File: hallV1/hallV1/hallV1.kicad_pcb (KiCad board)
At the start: 2 copper layers, 13 x 8 mm, 3 parts, among them J1 Conn_01x03_Female, U1 AH1806-Z

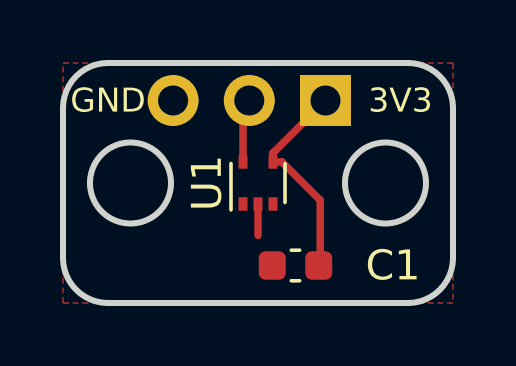
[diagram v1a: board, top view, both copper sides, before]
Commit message: Change decoupling capacitor position
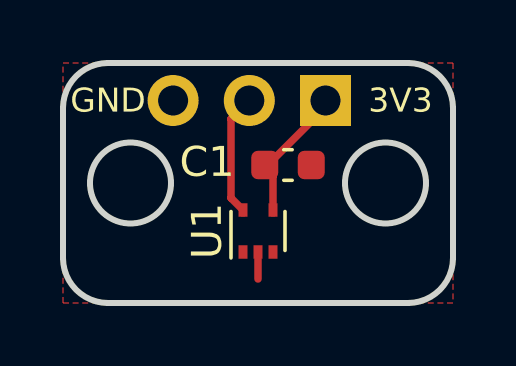
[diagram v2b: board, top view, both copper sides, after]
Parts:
- moved C1 3.36 mm to (105.2, 99.4), turned to 0 degrees
- moved U1 1.60 mm to (104.2, 101.6)
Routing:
- net +3V3: track 7.05 -> 4.70 mm
- net Net-(J1-Pad2): track 2.14 -> 4.47 mm
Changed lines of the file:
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@@
     (thickness 1)
     (drawings 13)
-    (tracks 8)
+    (tracks 10)
     (zones 0)
     (modules 3)
@@
     (aux_axis_origin 0 0)
     (grid_origin 97.75 104)
-    (visible_elements FFFFFF7F)
+    (visible_elements 7FFFFFFF)
     (pcbplotparams
       (layerselection 0x010fc_ffffffff)
@@
   )
   (module Capacitor_SMD:C_0603_1608Metric (layer F.Cu)
-    (at 105.5 102.75 180)
+    (at 105.25 99.4)
     (descr "Capacitor SMD 0603 (1608 Metric), square (rectangular) end terminal, IPC_7351 nominal, (Body size source: IPC-SM-782 page 76, https://www.pcb-3d.com/wordpress/wp-content/uploads/ipc-sm-782a_amendment_1_and_2.pdf), generated with kicad-footprint-generator")
     (tags capacitor)
     (attr smd)
-    (fp_text reference C1 (at -3.25 0) (layer F.SilkS)
+    (fp_text reference C1 (at -2.7 -0.1) (layer F.SilkS)
       (effects (font (size 1 1) (thickness 0.15)))
     )
@@
       (effects (font (size 1 1) (thickness 0.15)))
     )
+    (fp_line (start 1.48 0.73) (end -1.48 0.73) (layer F.CrtYd) (width 0.05))
+    (fp_line (start 1.48 -0.73) (end 1.48 0.73) (layer F.CrtYd) (width 0.05))
+    (fp_line (start -1.48 -0.73) (end 1.48 -0.73) (layer F.CrtYd) (width 0.05))
+    (fp_line (start -1.48 0.73) (end -1.48 -0.73) (layer F.CrtYd) (width 0.05))
+    (fp_line (start -0.14058 0.51) (end 0.14058 0.51) (layer F.SilkS) (width 0.12))
+    (fp_line (start -0.14058 -0.51) (end 0.14058 -0.51) (layer F.SilkS) (width 0.12))
+    (fp_line (start 0.8 0.4) (end -0.8 0.4) (layer F.Fab) (width 0.1))
+    (fp_line (start 0.8 -0.4) (end 0.8 0.4) (layer F.Fab) (width 0.1))
+    (fp_line (start -0.8 -0.4) (end 0.8 -0.4) (layer F.Fab) (width 0.1))
+    (fp_line (start -0.8 0.4) (end -0.8 -0.4) (layer F.Fab) (width 0.1))
     (fp_text user %R (at 0 0) (layer F.Fab)
       (effects (font (size 0.4 0.4) (thickness 0.06)))
     )
-    (fp_line (start -0.8 0.4) (end -0.8 -0.4) (layer F.Fab) (width 0.1))
-    (fp_line (start -0.8 -0.4) (end 0.8 -0.4) (layer F.Fab) (width 0.1))
-    (fp_line (start 0.8 -0.4) (end 0.8 0.4) (layer F.Fab) (width 0.1))
-    (fp_line (start 0.8 0.4) (end -0.8 0.4) (layer F.Fab) (width 0.1))
-    (fp_line (start -0.14058 -0.51) (end 0.14058 -0.51) (layer F.SilkS) (width 0.12))
-    (fp_line (start -0.14058 0.51) (end 0.14058 0.51) (layer F.SilkS) (width 0.12))
-    (fp_line (start -1.48 0.73) (end -1.48 -0.73) (layer F.CrtYd) (width 0.05))
-    (fp_line (start -1.48 -0.73) (end 1.48 -0.73) (layer F.CrtYd) (width 0.05))
-    (fp_line (start 1.48 -0.73) (end 1.48 0.73) (layer F.CrtYd) (width 0.05))
-    (fp_line (start 1.48 0.73) (end -1.48 0.73) (layer F.CrtYd) (width 0.05))
-    (pad 2 smd roundrect (at 0.775 0 180) (size 0.9 0.95) (layers F.Cu F.Paste F.Mask) (roundrect_rratio 0.25)
+    (pad 2 smd roundrect (at 0.775 0) (size 0.9 0.95) (layers F.Cu F.Paste F.Mask) (roundrect_rratio 0.25)
       (net 1 GND))
-    (pad 1 smd roundrect (at -0.775 0 180) (size 0.9 0.95) (layers F.Cu F.Paste F.Mask) (roundrect_rratio 0.25)
+    (pad 1 smd roundrect (at -0.775 0) (size 0.9 0.95) (layers F.Cu F.Paste F.Mask) (roundrect_rratio 0.25)
       (net 2 +3V3))
     (model ${KISYS3DMOD}/Capacitor_SMD.3dshapes/C_0603_1608Metric.wrl
@@
       (effects (font (size 1 1) (thickness 0.15)) (justify mirror))
     )
+    (fp_line (start -1.27 1.27) (end 0 1.27) (layer B.SilkS) (width 0.12))
     (fp_line (start -1.27 0) (end -1.27 1.27) (layer B.SilkS) (width 0.12))
-    (fp_line (start -1.27 1.27) (end 0 1.27) (layer B.SilkS) (width 0.12))
     (pad 3 thru_hole oval (at 0 -5.08 90) (size 1.7 1.7) (drill 1) (layers *.Cu *.Mask)
       (net 1 GND))
@@
   )
   (module Package_TO_SOT_SMD:SOT-553 (layer F.Cu)
-    (at 104.25 100 90)
+    (at 104.25 101.6 90)
     (descr SOT553)
     (tags SOT-553)
@@
       (effects (font (size 1 1) (thickness 0.15)))
     )
+    (fp_line (start 1.18 1.1) (end -1.18 1.1) (layer F.CrtYd) (width 0.05))
+    (fp_line (start 1.18 1.1) (end 1.18 -1.1) (layer F.CrtYd) (width 0.05))
+    (fp_line (start -1.18 -1.1) (end -1.18 1.1) (layer F.CrtYd) (width 0.05))
+    (fp_line (start -1.18 -1.1) (end 1.18 -1.1) (layer F.CrtYd) (width 0.05))
+    (fp_line (start 0.65 -0.85) (end -0.3 -0.85) (layer F.Fab) (width 0.1))
+    (fp_line (start 0.65 0.85) (end 0.65 -0.85) (layer F.Fab) (width 0.1))
+    (fp_line (start -0.65 0.85) (end 0.65 0.85) (layer F.Fab) (width 0.1))
+    (fp_line (start -0.65 -0.5) (end -0.65 0.85) (layer F.Fab) (width 0.1))
+    (fp_line (start -0.9 -0.9) (end 0.65 -0.9) (layer F.SilkS) (width 0.12))
+    (fp_line (start 0.65 0.9) (end -0.65 0.9) (layer F.SilkS) (width 0.12))
+    (fp_line (start -0.65 -0.5) (end -0.3 -0.85) (layer F.Fab) (width 0.1))
     (fp_text user %R (at 0 0 270) (layer F.Fab)
       (effects (font (size 0.4 0.4) (thickness 0.0625)))
     )
-    (fp_line (start -0.65 -0.5) (end -0.3 -0.85) (layer F.Fab) (width 0.1))
-    (fp_line (start 0.65 0.9) (end -0.65 0.9) (layer F.SilkS) (width 0.12))
-    (fp_line (start -0.9 -0.9) (end 0.65 -0.9) (layer F.SilkS) (width 0.12))
-    (fp_line (start -0.65 -0.5) (end -0.65 0.85) (layer F.Fab) (width 0.1))
-    (fp_line (start -0.65 0.85) (end 0.65 0.85) (layer F.Fab) (width 0.1))
-    (fp_line (start 0.65 0.85) (end 0.65 -0.85) (layer F.Fab) (width 0.1))
-    (fp_line (start 0.65 -0.85) (end -0.3 -0.85) (layer F.Fab) (width 0.1))
-    (fp_line (start -1.18 -1.1) (end 1.18 -1.1) (layer F.CrtYd) (width 0.05))
-    (fp_line (start -1.18 -1.1) (end -1.18 1.1) (layer F.CrtYd) (width 0.05))
-    (fp_line (start 1.18 1.1) (end 1.18 -1.1) (layer F.CrtYd) (width 0.05))
-    (fp_line (start 1.18 1.1) (end -1.18 1.1) (layer F.CrtYd) (width 0.05))
     (pad 4 smd rect (at 0.7 0.5 90) (size 0.45 0.3) (layers F.Cu F.Paste F.Mask)
       (net 2 +3V3))
@@
   (gr_arc (start 109.249999 97.500001) (end 110.75 97.500001) (angle -90) (layer Edge.Cuts) (width 0.2))
   (gr_circle (center 100 100) (end 101.35 100) (layer Edge.Cuts) (width 0.2))
-  (segment (start 104.25 100.7) (end 104.25 101.75) (width 0.25) (layer F.Cu) (net 1))
-  (segment (start 104.75 99) (end 106.5 97.25) (width 0.25) (layer F.Cu) (net 2))
-  (segment (start 104.75 99.3) (end 104.75 99) (width 0.25) (layer F.Cu) (net 2))
-  (segment (start 104.75 99.3) (end 105.05 99.3) (width 0.25) (layer F.Cu) (net 2))
-  (segment (start 106.325 100.575) (end 106.325 102.75) (width 0.25) (layer F.Cu) (net 2))
-  (segment (start 105.05 99.3) (end 106.325 100.575) (width 0.25) (layer F.Cu) (net 2))
+  (segment (start 104.25 102.3) (end 104.25 103.2) (width 0.25) (layer F.Cu) (net 1))
+  (segment (start 106.5 97.475) (end 104.475 99.5) (width 0.25) (layer F.Cu) (net 2))
+  (segment (start 106.5 97.25) (end 106.5 97.475) (width 0.25) (layer F.Cu) (net 2))
+  (segment (start 104.75 99.775) (end 104.75 101) (width 0.25) (layer F.Cu) (net 2))
+  (segment (start 104.475 99.5) (end 104.75 99.775) (width 0.25) (layer F.Cu) (net 2))
   (segment (start 103.75 97.46) (end 103.96 97.25) (width 0.25) (layer F.Cu) (net 3))
-  (segment (start 103.75 99.3) (end 103.75 97.46) (width 0.25) (layer F.Cu) (net 3))
+  (segment (start 103.75 100.9) (end 103.75 101) (width 0.25) (layer F.Cu) (net 3))
+  (segment (start 103.35 100.5) (end 103.75 100.9) (width 0.25) (layer F.Cu) (net 3))
+  (segment (start 103.35 97.86) (end 103.35 100.5) (width 0.25) (layer F.Cu) (net 3))
+  (segment (start 103.96 97.25) (end 103.35 97.86) (width 0.25) (layer F.Cu) (net 3))
   (zone (net 1) (net_name GND) (layer F.Cu) (hatch edge 0.508)
     (connect_pads yes (clearance 0.508))
